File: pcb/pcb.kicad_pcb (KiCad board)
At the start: 2 copper layers, 137.5 x 93.4 mm, 52 parts, among them SW1 SW_SPST, SW10 SW_SPST, SW11 SW_SPST, SW12 SW_SPST, SW13 SW_SPST, SW14 SW_SPST, SW15 SW_SPST, SW16 SW_SPST, SW17 SW_SPST, SW18 SW_SPST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

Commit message: перевернул
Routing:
- net R3: track 128.5 -> 130.4 mm

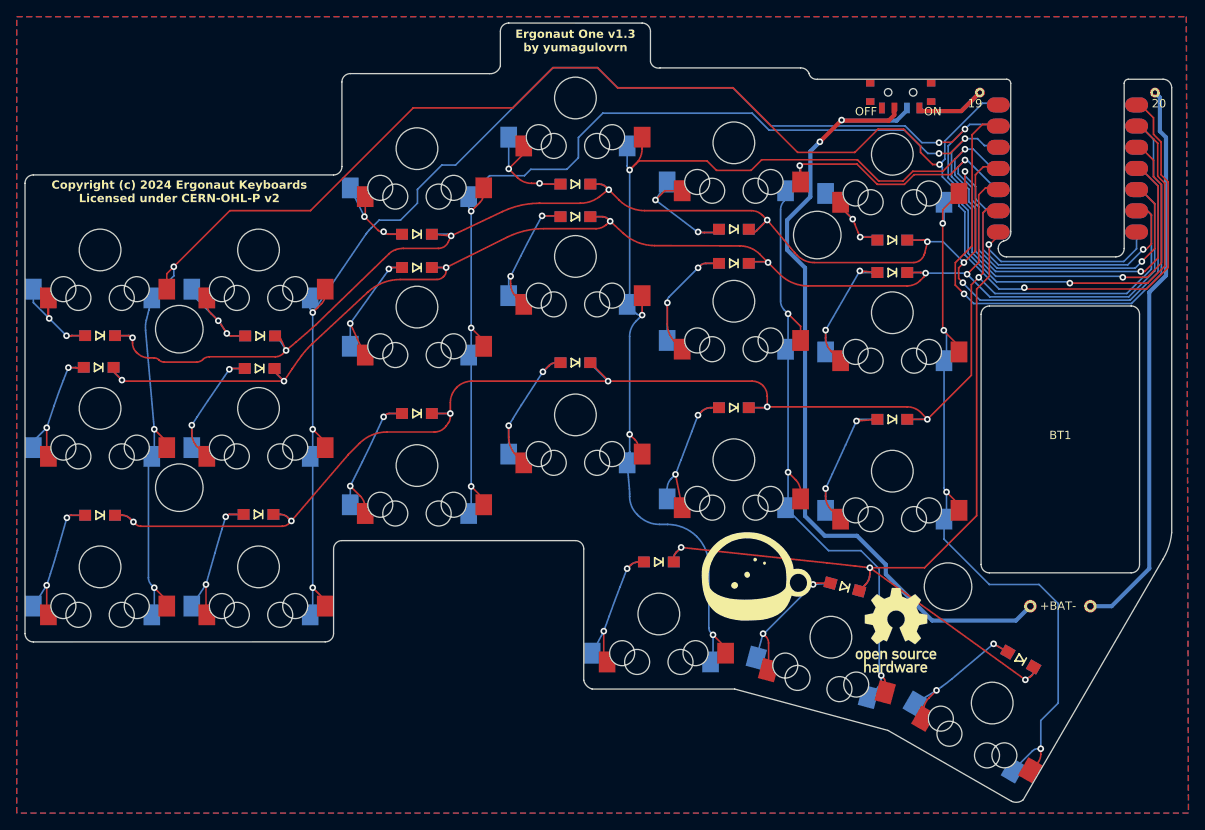
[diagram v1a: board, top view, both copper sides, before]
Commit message: провода нарисовал
Размеры поправил
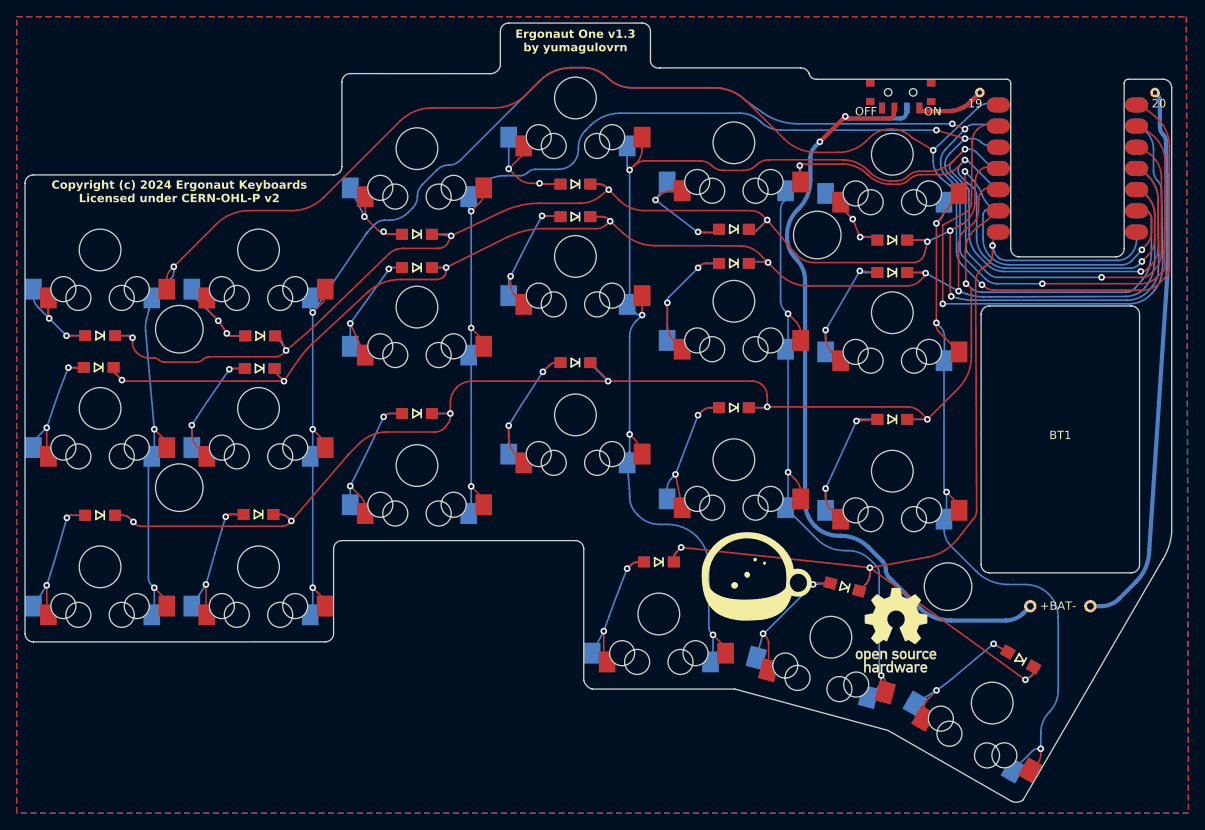
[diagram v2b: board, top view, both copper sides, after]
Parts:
- U1: footprint Two:XIAO_nRF52840_DUAL_WINDOW -> Two:XIAO_nRF52840_DUAL_WINDOW_NO_CAP
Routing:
- net C2: track 171.0 -> 166.2 mm
- net C0: track 229.8 -> 225.4 mm
- net C4: track 152.4 -> 149.4 mm
- net GND: track 68.4 -> 71.3 mm
- net C1: track 205.1 -> 202.6 mm
- net C5: track 132.8 -> 130.4 mm
- net Net-(BT1-+): track 100.5 -> 98.7 mm
- net R3: track 130.4 -> 128.7 mm
- net R1: track 183.4 -> 185.0 mm
- net C3: track 175.2 -> 173.7 mm
- net Net-(BT1--): track 67.4 -> 66.1 mm
- net Net-(D1-A): track 16.8 -> 15.9 mm
- net R0: track 199.6 -> 198.9 mm
